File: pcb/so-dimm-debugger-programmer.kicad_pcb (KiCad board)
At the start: 2 copper layers, 48.9 x 131.2 mm, 51 parts, among them J1 1612618-4, J10 Conn_01x08_Pin, J12 Conn_01x06_Pin, J13 Conn_01x04_Pin, J2 Conn_01x06_Pin, J3 Conn_01x04_Pin, J4 Conn_01x04_Pin, J5 Conn_01x08_Pin, J6 USB4105-GF-A, J7 USB4105-GF-A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

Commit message: Fix E1_IO0_3 connected to Pin 22 instead of 23
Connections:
- J1 pad 22: /E1_IO0_03 -> unconnected-(J1-Pad22)
- J1 pad 23: unconnected-(J1-Pad23) -> /E1_IO0_03
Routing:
- net /E1_IO0_03: track 48.8 -> 45.6 mm

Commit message: Fix font issue with KiCad returning to default font
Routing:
- net GND: vias 26 -> 22

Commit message: Fix unconnected plane
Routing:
- net /EN: track 165.5 -> 165.8 mm, vias 2 -> 4
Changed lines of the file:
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@@
   (segment (start 105.210205 138.911547) (end 104.613205 138.314547) (width 0.25) (layer "F.Cu") (net 176))
   (segment (start 135.436205 152.577047) (end 132.993705 152.577047) (width 0.25) (layer "F.Cu") (net 176))
+  (segment (start 95.671752 62.611) (end 95.758 62.611) (width 0.25) (layer "F.Cu") (net 176))
   (segment (start 107.242205 137.019547) (end 106.846205 137.415547) (width 0.25) (layer "F.Cu") (net 176))
   (segment (start 132.993705 152.577047) (end 132.870205 152.453547) (width 0.25) (layer "F.Cu") (net 176))
@@
   (segment (start 94.154205 123.310547) (end 95.685205 121.779547) (width 0.25) (layer "F.Cu") (net 176))
   (segment (start 110.036205 137.019547) (end 107.242205 137.019547) (width 0.25) (layer "F.Cu") (net 176))
-  (segment (start 109.232205 49.050547) (end 112.618205 49.050547) (width 0.25) (layer "F.Cu") (net 176))
+  (segment (start 109.232205 49.050547) (end 109.22 49.022) (width 0.25) (layer "F.Cu") (net 176))
   (segment (start 112.618205 49.050547) (end 115.751205 52.183547) (width 0.25) (layer "F.Cu") (net 176))
   (segment (start 118.941205 58.675547) (end 120.100205 58.675547) (width 0.25) (layer "F.Cu") (net 176))
@@
   (segment (start 94.154205 133.336547) (end 95.177205 133.336547) (width 0.25) (layer "F.Cu") (net 176))
   (segment (start 115.751205 55.485547) (end 118.941205 58.675547) (width 0.25) (layer "F.Cu") (net 176))
-  (segment (start 95.685205 62.597547) (end 109.232205 49.050547) (width 0.25) (layer "F.Cu") (net 176))
+  (segment (start 95.685205 62.597547) (end 95.671752 62.611) (width 0.25) (layer "F.Cu") (net 176))
   (segment (start 95.685205 121.779547) (end 95.685205 62.597547) (width 0.25) (layer "F.Cu") (net 176))
   (segment (start 106.846205 137.415547) (end 106.846205 138.863547) (width 0.25) (layer "F.Cu") (net 176))
   (segment (start 122.656205 144.559547) (end 117.576205 144.559547) (width 0.25) (layer "F.Cu") (net 176))
+  (segment (start 109.22 49.022) (end 112.618205 49.050547) (width 0.25) (layer "F.Cu") (net 176))
   (segment (start 115.751205 52.183547) (end 115.751205 55.485547) (width 0.25) (layer "F.Cu") (net 176))
   (segment (start 105.210205 138.911547) (end 106.798205 138.911547) (width 0.25) (layer "F.Cu") (net 176))
   (segment (start 128.578205 150.481547) (end 128.578205 145.274547) (width 0.25) (layer "F.Cu") (net 176))
   (segment (start 95.177205 133.336547) (end 95.304205 133.209547) (width 0.25) (layer "F.Cu") (net 176))
+  (segment (start 95.758 62.611) (end 95.758 62.524752) (width 0.25) (layer "F.Cu") (net 176))
   (segment (start 95.329205 138.314547) (end 94.154205 137.139547) (width 0.25) (layer "F.Cu") (net 176))
   (segment (start 106.798205 138.911547) (end 106.846205 138.863547) (width 0.25) (layer "F.Cu") (net 176))
+  (via (at 95.758 62.611) (size 0.8) (drill 0.4) (layers "F.Cu" "B.Cu") (net 176))
+  (via (at 109.22 49.022) (size 0.8) (drill 0.4) (layers "F.Cu" "B.Cu") (net 176))
   (via (at 122.656205 144.559547) (size 0.6) (drill 0.3) (layers "F.Cu" "B.Cu") (net 176))
   (via (at 128.578205 145.274547) (size 0.6) (drill 0.3) (layers "F.Cu" "B.Cu") (net 176))
   (segment (start 128.578205 145.274547) (end 127.863205 144.559547) (width 0.25) (layer "B.Cu") (net 176))
   (segment (start 127.863205 144.559547) (end 122.656205 144.559547) (width 0.25) (layer "B.Cu") (net 176))
+  (segment (start 109.22 49.022) (end 95.758 62.484) (width 0.25) (layer "B.Cu") (net 176))
+  (segment (start 95.758 62.484) (end 95.758 62.611) (width 0.25) (layer "B.Cu") (net 176))
   (segment (start 110.150205 160.655547) (end 111.433205 159.372547) (width 0.5) (layer "F.Cu") (net 178))
   (segment (start 107.750205 157.430547) (end 107.750205 158.005547) (width 0.2) (layer "F.Cu") (net 178))

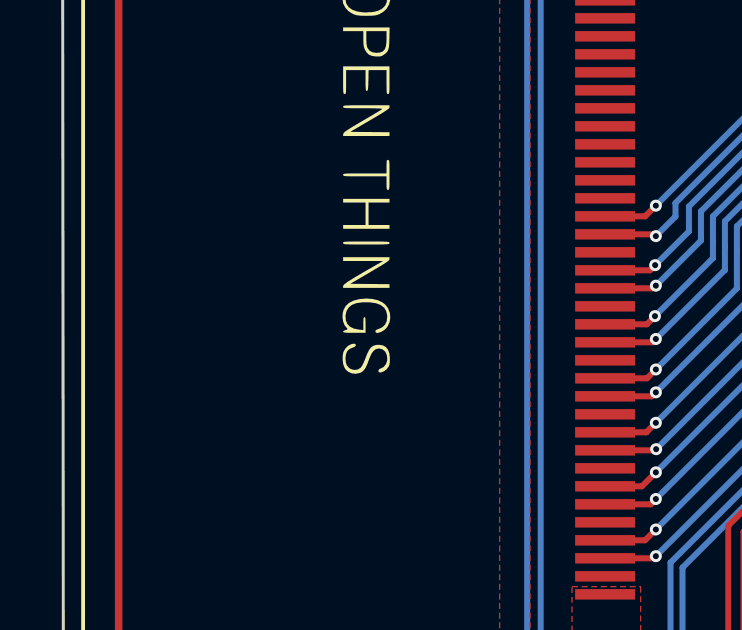
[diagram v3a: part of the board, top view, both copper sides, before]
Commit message: Added revision silk to top layer
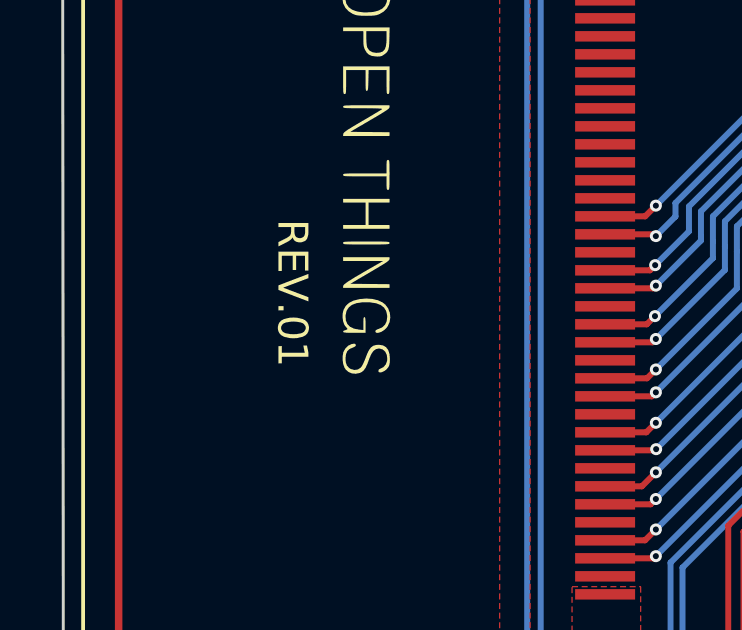
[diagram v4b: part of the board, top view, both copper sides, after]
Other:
- board text added: "REV.01"
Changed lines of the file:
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@@
     (effects (font (size 0.8 0.8) (thickness 0.15) bold))
+  )
+  (gr_text "REV.01" (at 100.8888 86.6648 -90) (layer "F.SilkS")
+    (effects (font (size 1 1) (thickness 0.15)) (justify left bottom))
   )
   (gr_text "IO02" (at 117.011428 148.449547) (layer "F.SilkS" knockout)

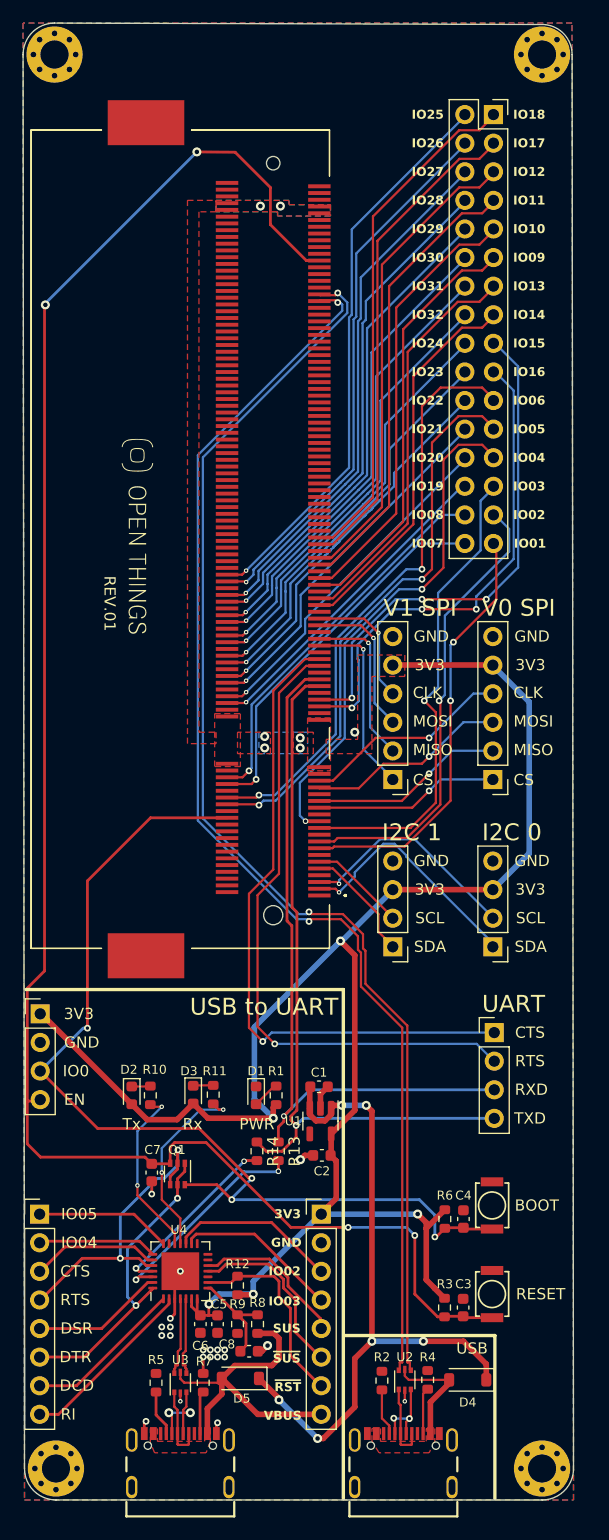
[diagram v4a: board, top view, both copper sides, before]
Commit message: Fix copper to edge issue
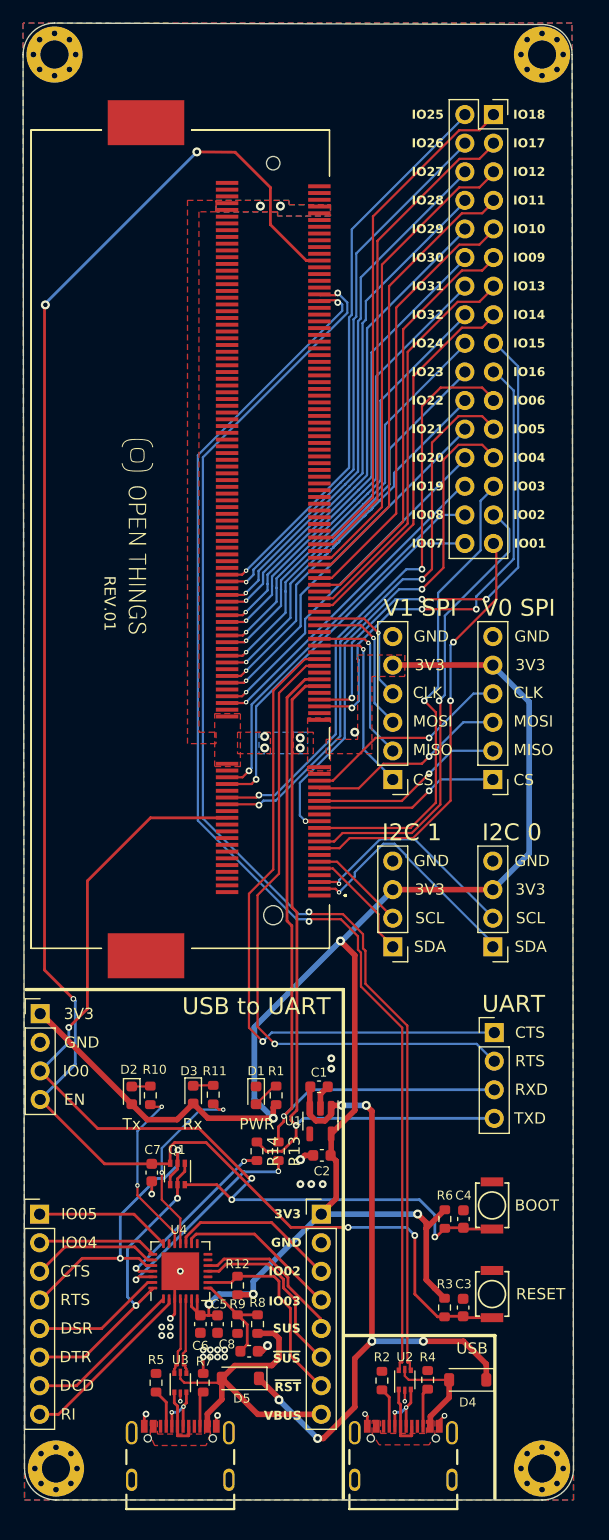
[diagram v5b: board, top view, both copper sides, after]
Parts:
- moved J7 0.65 mm to (107.7, 167.0)
- moved J6 0.65 mm to (127.6, 167.0)
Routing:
- net /usb-ports/CP_D-: track 8.54 -> 5.64 mm
- net /EN: track 165.8 -> 163.1 mm, vias 4 -> 5
- net GND: track 15.8 -> 18.1 mm, vias 22 -> 29
- net /usb-ports/USB_D-: track 7.16 -> 5.88 mm
- net /usb-ports/USB_D+: track 6.81 -> 6.01 mm
- net /usb-ports/CP_D+: track 6.60 -> 5.81 mm
- net Net-(J6-CC1): track 4.28 -> 3.50 mm
- net Net-(J7-CC1): track 4.19 -> 3.42 mm
- net Net-(J7-CC2): track 3.93 -> 3.16 mm
- net VBUS: track 29.9 -> 29.1 mm
- net Net-(J6-CC2): track 4.24 -> 3.47 mm
- net /usb-ports/VBUSB: track 10.2 -> 9.47 mm
